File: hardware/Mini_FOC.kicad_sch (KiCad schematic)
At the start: 41 parts, among them J1 Conn_01x03_Socket, J2 Conn_01x06_Socket, J3 Conn_01x04_Socket, J4 Conn_01x04_Socket, J5 Conn_01x02_Socket, J6 Conn_01x06_Socket, SW1 SW_SPDT, U1 DRV8313PWPR, U2 STM32F103C8T6, U3 AMS1117-3.3, U4 LM2596SX-5.0/NOPB, Y2 8MHz

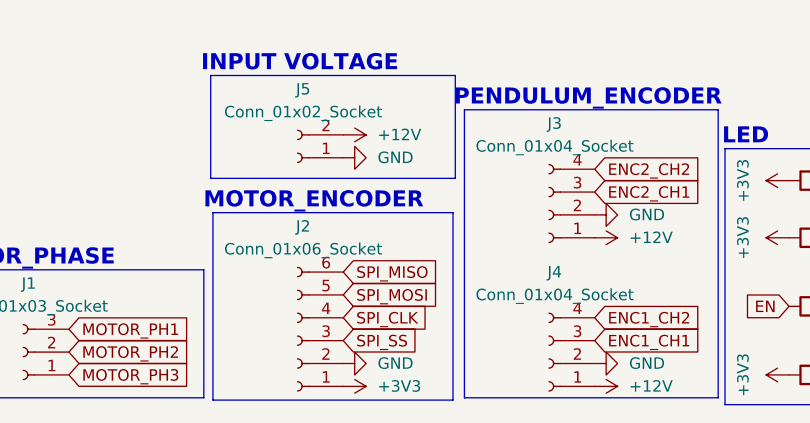
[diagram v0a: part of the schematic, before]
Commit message: minimize the pcb & add logo
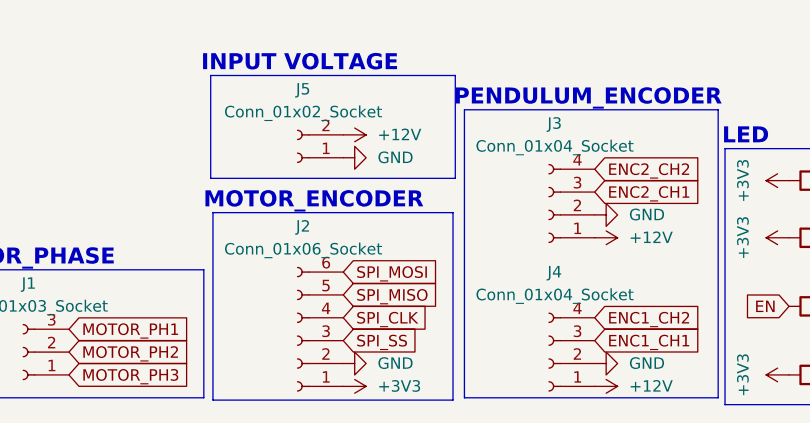
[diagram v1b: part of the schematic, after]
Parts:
- J2: footprint Connector_JST:JST_XH_B6B-XH-A_1x06_P2.50mm_Vertical -> Connector_JST:JST_ZH_B6B-ZR_1x06_P1.50mm_Vertical
- J3, J4: footprint Connector_JST:JST_XH_B4B-XH-A_1x04_P2.50mm_Vertical -> Connector_JST:JST_ZH_B4B-ZR_1x04_P1.50mm_Vertical
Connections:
- net SPI_MISO: now also J2.5 (Pin_5); no longer J2.6 (Pin_6)
- net SPI_MOSI: now also J2.6 (Pin_6); no longer J2.5 (Pin_5)
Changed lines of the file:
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@@
 	(global_label "SPI_MISO"
 		(shape input)
-		(at 86.36 181.61 0)
+		(at 86.36 184.15 0)
 		(fields_autoplaced yes)
 		(effects
@@
 		)
 		(property "Intersheetrefs" "${INTERSHEET_REFS}"
-			(at 97.9933 181.61 0)
+			(at 97.9933 184.15 0)
 			(effects
 				(font
@@
 	(global_label "SPI_MOSI"
 		(shape input)
-		(at 86.36 184.15 0)
+		(at 86.36 181.61 0)
 		(fields_autoplaced yes)
 		(effects
@@
 		)
 		(property "Intersheetrefs" "${INTERSHEET_REFS}"
-			(at 97.9933 184.15 0)
+			(at 97.9933 181.61 0)
 			(effects
 				(font
@@
 			)
 		)
-		(property "Footprint" "Connector_JST:JST_XH_B4B-XH-A_1x04_P2.50mm_Vertical"
+		(property "Footprint" "Connector_JST:JST_ZH_B4B-ZR_1x04_P1.50mm_Vertical"
 			(at 109.22 175.26 0)
 			(effects
@@
 			)
 		)
-		(property "Footprint" "Connector_JST:JST_XH_B4B-XH-A_1x04_P2.50mm_Vertical"
+		(property "Footprint" "Connector_JST:JST_ZH_B4B-ZR_1x04_P1.50mm_Vertical"
 			(at 109.22 191.77 0)
 			(effects
@@
 			)
 		)
-		(property "Footprint" "Connector_JST:JST_XH_B6B-XH-A_1x06_P2.50mm_Vertical"
+		(property "Footprint" "Connector_JST:JST_ZH_B6B-ZR_1x06_P1.50mm_Vertical"
 			(at 81.28 189.23 0)
 			(effects

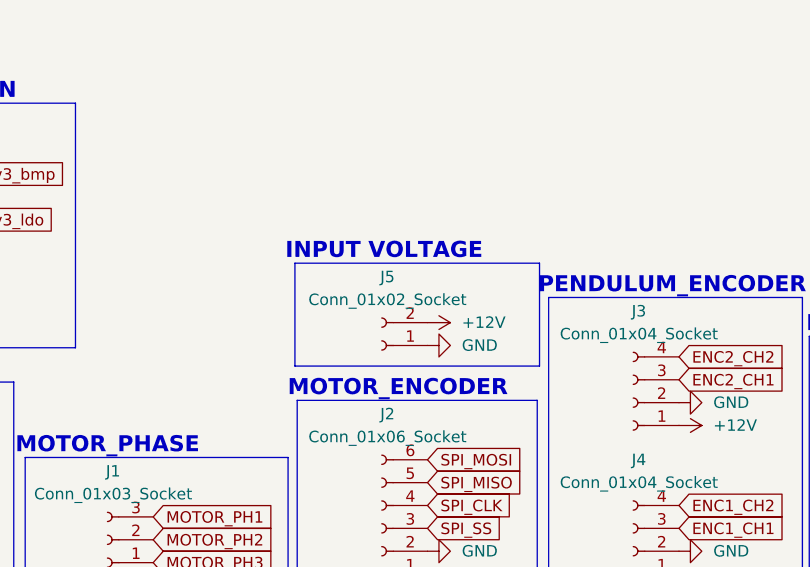
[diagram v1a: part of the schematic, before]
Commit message: replace power connector
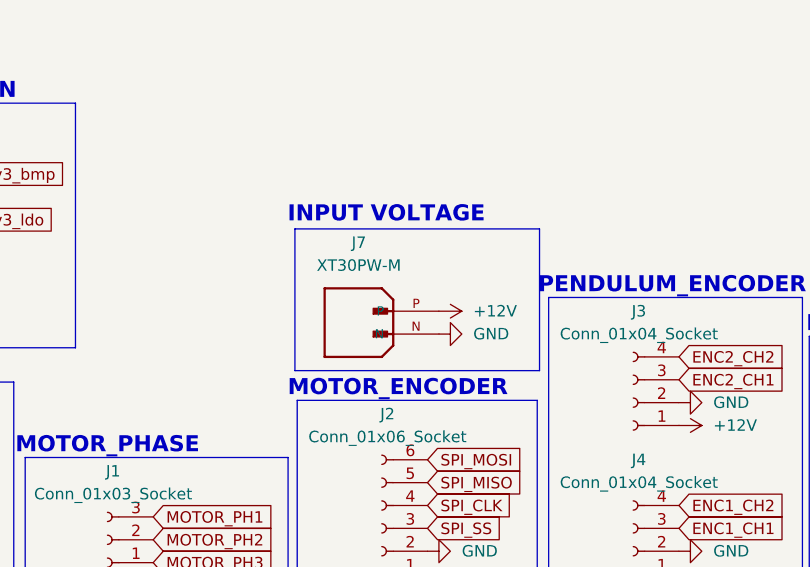
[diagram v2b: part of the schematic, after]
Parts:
- removed J5: Conn_01x02_Socket, TerminalBlock:TerminalBlock_bornier-2_P5.08mm, symbol Connector:Conn_01x02_Socket
- added J7: XT30PW-M, tue_xt30pw-m:AMASS_XT30PW-M, symbol tue_xt30pw-m:XT30PW-M
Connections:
- net +12V: now also J7.P
- net GND: now also J7.N
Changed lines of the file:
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@@
 	(paper "A4")
 	(rectangle
-		(start 71.628 159.766)
-		(end 98.806 171.196)
+		(start 71.628 155.956)
+		(end 98.806 171.704)
 		(stroke
 			(width 0)
@@
 	(text "INPUT VOLTAGE"
 		(exclude_from_sim no)
-		(at 81.534 158.496 0)
+		(at 81.788 154.432 0)
 		(effects
 			(font
@@
 	)
 	(symbol
-		(lib_id "Connector:Conn_01x02_Socket")
-		(at 81.28 168.91 180)
-		(unit 1)
-		(exclude_from_sim no)
-		(in_bom yes)
-		(on_board yes)
-		(dnp no)
-		(fields_autoplaced yes)
-		(property "Reference" "J5"
-			(at 81.915 161.29 0)
-			(effects
-				(font
-					(size 1.27 1.27)
-				)
-			)
-		)
-		(property "Value" "Conn_01x02_Socket"
-			(at 81.915 163.83 0)
-			(effects
-				(font
-					(size 1.27 1.27)
-				)
-			)
-		)
-		(property "Footprint" "TerminalBlock:TerminalBlock_bornier-2_P5.08mm"
-			(at 81.28 168.91 0)
-			(effects
-				(font
-					(size 1.27 1.27)
-				)
-				(hide yes)
-			)
-		)
-		(property "Datasheet" "~"
-			(at 81.28 168.91 0)
-			(effects
-				(font
-					(size 1.27 1.27)
-				)
-				(hide yes)
-			)
-		)
-		(property "Description" "Generic connector, single row, 01x02, script generated"
-			(at 81.28 168.91 0)
-			(effects
-				(font
-					(size 1.27 1.27)
-				)
-				(hide yes)
-			)
-		)
-		(pin "1"
-		)
-		(pin "2"
-		)
-		(instances
-			(project ""
-				(path "/ee8eccf0-1ae2-4f56-935e-466680668989"
-					(reference "J5")
-					(unit 1)
-				)
-			)
-		)
-	)
-	(symbol
 		(lib_id "Device:C")
 		(at 361.95 50.8 0)
@@
 	(symbol
 		(lib_id "power:GND")
-		(at 86.36 168.91 90)
+		(at 87.63 167.64 90)
 		(unit 1)
 		(exclude_from_sim no)
@@
 		(fields_autoplaced yes)
 		(property "Reference" "#PWR041"
-			(at 92.71 168.91 0)
+			(at 93.98 167.64 0)
 			(effects
 				(font
@@
 		)
 		(property "Value" "GND"
-			(at 90.17 168.9099 90)
+			(at 91.44 167.6399 90)
 			(effects
 				(font
@@
 		)
 		(property "Footprint" ""
-			(at 86.36 168.91 0)
+			(at 87.63 167.64 0)
 			(effects
 				(font
@@
 		)
 		(property "Datasheet" ""
-			(at 86.36 168.91 0)
+			(at 87.63 167.64 0)
 			(effects
 				(font
@@
 		)
 		(property "Description" "Power symbol creates a global label with name \"GND\" , ground"
-			(at 86.36 168.91 0)
+			(at 87.63 167.64 0)
 			(effects
 				(font
@@
 	)
 	(symbol
+		(lib_id "tue_xt30pw-m:XT30PW-M")
+		(at 82.55 165.1 0)
+		(unit 1)
+		(exclude_from_sim no)
+		(in_bom yes)
+		(on_board yes)
+		(dnp no)
+		(fields_autoplaced yes)
+		(property "Reference" "J7"
+			(at 78.74 157.48 0)
+			(effects
+				(font
+					(size 1.27 1.27)
+				)
+			)
+		)
+		(property "Value" "XT30PW-M"
+			(at 78.74 160.02 0)
+			(effects
+				(font
+					(size 1.27 1.27)
+				)
+			)
+		)
+		(property "Footprint" "tue_xt30pw-m:AMASS_XT30PW-M"
+			(at 82.55 165.1 0)
+			(effects
+				(font
+					(size 1.27 1.27)
+				)
+				(justify bottom)
+				(hide yes)
+			)
+		)
+		(property "Datasheet" ""
+			(at 82.55 165.1 0)
+			(effects
+				(font
+					(size 1.27 1.27)
+				)
+				(hide yes)
+			)
+		)
+		(property "Description" ""
+			(at 82.55 165.1 0)
+			(effects
+				(font
+					(size 1.27 1.27)
+				)
+				(hide yes)
+			)
+		)
+		(property "MF" "AMASS"
+			(at 82.55 165.1 0)
+			(effects
+				(font
+					(size 1.27 1.27)
+				)
+				(justify bottom)
+				(hide yes)
+			)
+		)
+		(property "MAXIMUM_PACKAGE_HEIGHT" "5 mm"
+			(at 82.55 165.1 0)
+			(effects
+				(font
+					(size 1.27 1.27)
+				)
+				(justify bottom)
+				(hide yes)
+			)
+		)
+		(property "Package" "None"
+			(at 82.55 165.1 0)
+			(effects
+				(font
+					(size 1.27 1.27)
+				)
+				(justify bottom)
+				(hide yes)
+			)
+		)
+		(property "Price" "None"
+			(at 82.55 165.1 0)
+			(effects
+				(font
+					(size 1.27 1.27)
+				)
+				(justify bottom)
+				(hide yes)
+			)
+		)
+		(property "Check_prices" "https://www.snapeda.com/parts/XT30PW-M/AMASS/view-part/?ref=eda"
+			(at 82.55 165.1 0)
+			(effects
+				(font
+					(size 1.27 1.27)
+				)
+				(justify bottom)
+				(hide yes)
+			)
+		)
+		(property "STANDARD" "Manufacturer Recommendations"
+			(at 82.55 165.1 0)
+			(effects
+				(font
+					(size 1.27 1.27)
+				)
+				(justify bottom)
+				(hide yes)
+			)
+		)
+		(property "PARTREV" "1.2"
+			(at 82.55 165.1 0)
+			(effects
+				(font
+					(size 1.27 1.27)
+				)
+				(justify bottom)
+				(hide yes)
+			)
+		)
+		(property "SnapEDA_Link" "https://www.snapeda.com/parts/XT30PW-M/AMASS/view-part/?ref=snap"
+			(at 82.55 165.1 0)
+			(effects
+				(font
+					(size 1.27 1.27)
+				)
+				(justify bottom)
+				(hide yes)
+			)
+		)
+		(property "MP" "XT30PW-M"
+			(at 82.55 165.1 0)
+			(effects
+				(font
+					(size 1.27 1.27)
+				)
+				(justify bottom)
+				(hide yes)
+			)
+		)
+		(property "Description_1" "Socket; DC supply; XT30; male; PIN: 2; on PCBs; THT; Colour: yellow"
+			(at 82.55 165.1 0)
+			(effects
+				(font
+					(size 1.27 1.27)
+				)
+				(justify bottom)
+				(hide yes)
+			)
+		)
+		(property "MANUFACTURER" "Amass"
+			(at 82.55 165.1 0)
+			(effects
+				(font
+					(size 1.27 1.27)
+				)
+				(justify bottom)
+				(hide yes)
+			)
+		)
+		(property "Availability" "In Stock"
+			(at 82.55 165.1 0)
+			(effects
+				(font
+					(size 1.27 1.27)
+				)
+				(justify bottom)
+				(hide yes)
+			)
+		)
+		(property "SNAPEDA_PN" "XT30PW-M"
+			(at 82.55 165.1 0)
+			(effects
+				(font
+					(size 1.27 1.27)
+				)
+				(justify bottom)
+				(hide yes)
+			)
+		)
+		(pin "P"
+		)
+		(pin "N"
+		)
+		(instances
+			(project ""
+				(path "/ee8eccf0-1ae2-4f56-935e-466680668989"
+					(reference "J7")
+					(unit 1)
+				)
+			)
+		)
+	)
+	(symbol
 		(lib_id "power:GND")
 		(at 236.22 123.19 90)
@@
 	(symbol
 		(lib_id "power:+12V")
-		(at 86.36 166.37 270)
+		(at 87.63 165.1 270)
 		(unit 1)
 		(exclude_from_sim no)
@@
 		(fields_autoplaced yes)
 		(property "Reference" "#PWR040"
-			(at 82.55 166.37 0)
+			(at 83.82 165.1 0)
 			(effects
 				(font
@@
 		)
 		(property "Value" "+12V"
-			(at 90.17 166.3699 90)
+			(at 91.44 165.0999 90)
 			(effects
 				(font
@@
 		)
 		(property "Footprint" ""
-			(at 86.36 166.37 0)
+			(at 87.63 165.1 0)
 			(effects
 				(font
@@
 		)
 		(property "Datasheet" ""
-			(at 86.36 166.37 0)
+			(at 87.63 165.1 0)
 			(effects
 				(font
@@
 		)
 		(property "Description" "Power symbol creates a global label with name \"+12V\""
-			(at 86.36 166.37 0)
+			(at 87.63 165.1 0)
 			(effects
 				(font
